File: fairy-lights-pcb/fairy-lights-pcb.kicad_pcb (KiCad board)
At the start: 2 copper layers, 60 x 60 mm, 19 parts, among them J1 Power_Jack, J2 Conn_LED_Strand_SPI, J3 Conn_LED_Strand_WS2812, J4 Conn_I2C, J5 Conn_02x04_Top_Bottom, SW1 SW_PWR, SW2 USER_A, SW3 USER_B, U1 WeMos_D1_mini

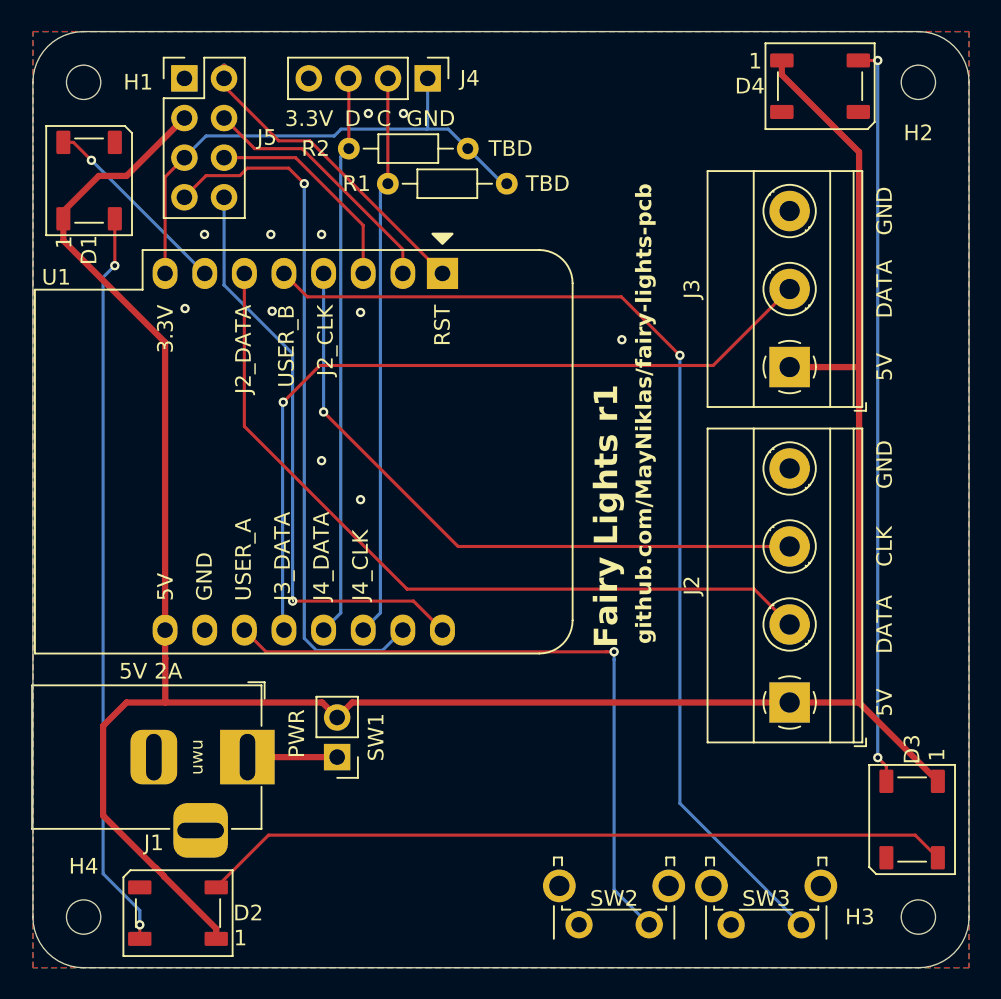
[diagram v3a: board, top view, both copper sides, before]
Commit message: Tweak MCU pin assignment
- Swaps the J3_DATA and USER_B pins.
- Now, all LED strand terminals and the I2C header are connected to GPIO
  pins with no strings (or, more accurately, random components on the
  MCU module) attached.
- Button USER_B puts the MCU flash mode if pressed at boot-up. The same
  can be achieved via USB, but, I guess, it's useful for flashing in the
  field with no USB but a UART?
- Button USER_A is tied to the same pin that drives the MCU module's
  on-board LED. When USER_A is pressed, the LED lights up. It might be
  worthwhile to re-wire USER_A to MCU pin D0 in order to free the LED
  and allow using USER_A as a soft power button (although that would
  require regularly polling the button in software while the MCU is
  running).
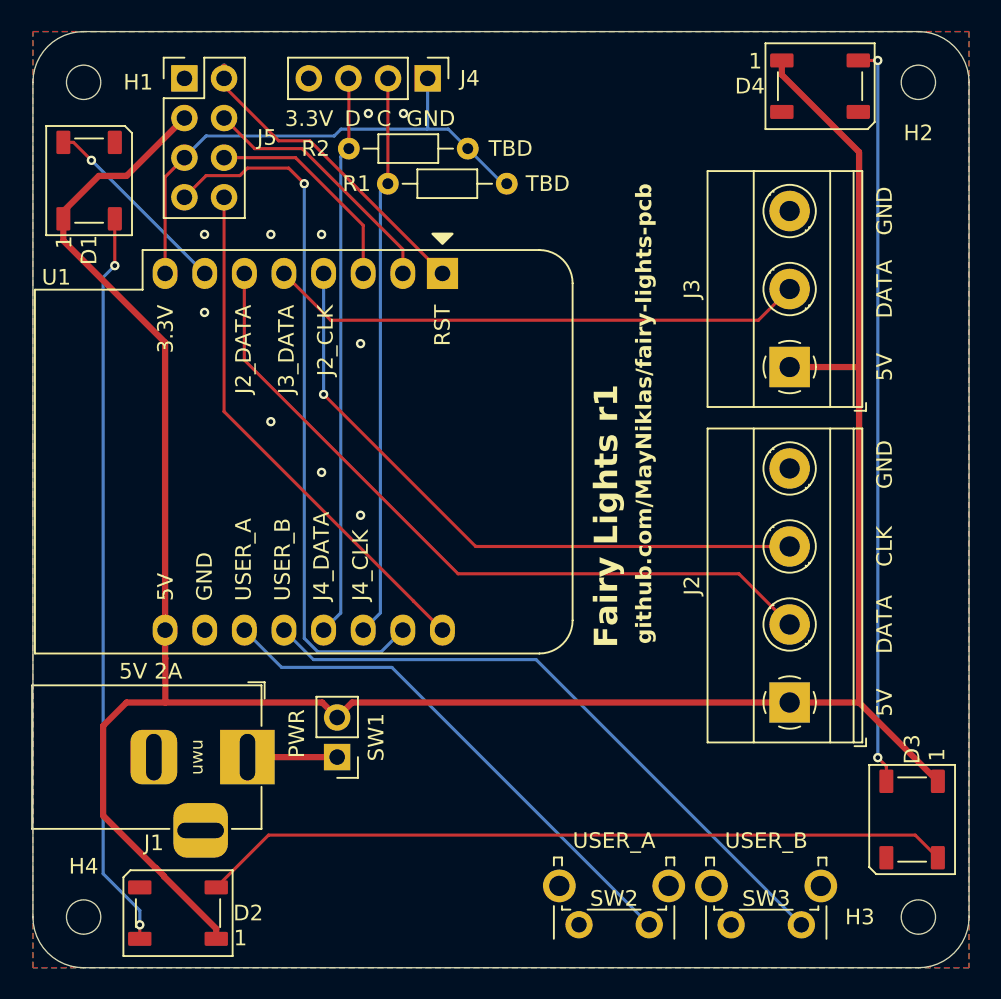
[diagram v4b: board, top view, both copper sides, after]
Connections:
- SW3 pad 1: Net-(U1-MISO/D6) -> Net-(U1-D3)
- U1 pad 12: Net-(J3-DATA) -> Net-(U1-D3)
- U1 pad 5: Net-(U1-MISO/D6) -> Net-(J3-DATA)
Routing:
- net Net-(U1-MISO/D6): track 67.3 -> 0.00 mm, vias 1 -> 0
- net Net-(U1-D3): track 0.00 -> 41.1 mm
- net Net-(J3-DATA): track 50.1 -> 34.5 mm, vias 1 -> 0
- net Net-(U1-D4): track 42.7 -> 33.8 mm, vias 1 -> 0
- net UC_TX: track 38.1 -> 33.5 mm, vias 1 -> 0
- net Net-(J2-DATA): track 50.0 -> 47.5 mm
- net Net-(J2-CLK): track 42.3 -> 41.7 mm
- net GND: vias 11 -> 10
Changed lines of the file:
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@@
 	(net 12 "UC_A0")
 	(net 13 "UC_D0")
-	(net 14 "Net-(U1-MISO{slash}D6)")
+	(net 14 "Net-(U1-D3)")
 	(net 15 "Net-(U1-D4)")
 	(net 16 "Net-(J4-CLK)")
@@
 		(property "Value" "USER_A"
 			(at 2.25 5.38988 180)
-			(layer "F.Fab")
+			(layer "F.SilkS")
 			(effects
 				(font
@@
 			(layers "*.Cu" "*.Mask")
 			(remove_unused_layers no)
-			(net 14 "Net-(U1-MISO{slash}D6)")
+			(net 6 "Net-(J3-DATA)")
 			(pinfunction "MISO/D6")
 			(pintype "bidirectional")
@@
 			(layers "*.Cu" "*.Mask")
 			(remove_unused_layers no)
-			(net 6 "Net-(J3-DATA)")
+			(net 14 "Net-(U1-D3)")
 			(pinfunction "D3")
 			(pintype "bidirectional")
@@
 		(property "Value" "USER_B"
 			(at 2.25 5.38988 180)
-			(layer "F.Fab")
+			(layer "F.SilkS")
 			(effects
 				(font
@@
 			(layers "*.Cu" "*.Mask")
 			(remove_unused_layers no)
-			(net 14 "Net-(U1-MISO{slash}D6)")
+			(net 14 "Net-(U1-D3)")
 			(pinfunction "1")
 			(pintype "passive")
@@
 		)
 	)
-	(gr_text "USER_B"
+	(gr_text "J3_DATA"
 		(at 76.25 77.5 90)
 		(layer "F.SilkS")
@@
 		)
 	)
-	(gr_text "J3_DATA"
+	(gr_text "USER_B"
 		(at 76 96.5 90)
 		(layer "F.SilkS")
@@
 	)
 	(via
-		(at 81 78)
+		(at 75.25 85)
 		(size 0.6)
 		(drill 0.3)
@@
 	)
 	(via
-		(at 75.332107 77.917893)
+		(at 78.5 73)
 		(size 0.6)
 		(drill 0.3)
@@
 	)
 	(via
-		(at 78.5 87.5)
+		(at 78.5 88.25)
 		(size 0.6)
 		(drill 0.3)
@@
 	)
 	(via
-		(at 78.5 73)
+		(at 81.5 65.25)
 		(size 0.6)
 		(drill 0.3)
@@
 	)
 	(via
-		(at 81.5 65.25)
+		(at 81 80)
 		(size 0.6)
 		(drill 0.3)
@@
 	)
 	(via
-		(at 71 73)
+		(at 81 91)
 		(size 0.6)
 		(drill 0.3)
@@
 	)
 	(via
-		(at 97.75 79.75)
+		(at 71 73)
 		(size 0.6)
 		(drill 0.3)
@@
 	)
 	(via
-		(at 69.75 77.75)
+		(at 71 78)
 		(size 0.6)
 		(drill 0.3)
@@
 		(net 2)
 	)
-	(via
-		(at 81 90)
-		(size 0.6)
-		(drill 0.3)
-		(layers "F.Cu" "B.Cu")
-		(free yes)
-		(net 2)
-	)
 	(segment
-		(start 83.983 95.733)
-		(end 73.55 85.3)
+		(start 108.5 98)
+		(end 105.25 94.75)
 		(width 0.2)
 		(layer "F.Cu")
@@
 	)
 	(segment
-		(start 108.5 98)
-		(end 106.233 95.733)
+		(start 73.55 81.05)
+		(end 73.55 75.5)
 		(width 0.2)
 		(layer "F.Cu")
@@
 	)
 	(segment
-		(start 73.55 85.3)
-		(end 73.55 75.5)
+		(start 87.25 94.75)
+		(end 73.55 81.05)
 		(width 0.2)
 		(layer "F.Cu")
@@
 	)
 	(segment
-		(start 106.233 95.733)
-		(end 83.983 95.733)
+		(start 105.25 94.75)
+		(end 87.25 94.75)
 		(width 0.2)
 		(layer "F.Cu")
@@
 	)
 	(segment
-		(start 87.25 93)
+		(start 88.38 93)
 		(end 108.5 93)
 		(width 0.2)
@@
 	)
 	(segment
-		(start 78.63 84.38)
-		(end 87.25 93)
+		(start 78.63 83.25)
+		(end 88.38 93)
 		(width 0.2)
 		(layer "F.Cu")
@@
 	)
 	(via
-		(at 78.63 84.38)
+		(at 78.63 83.25)
 		(size 0.6)
 		(drill 0.3)
@@
 	)
 	(segment
-		(start 78.63 84.38)
+		(start 78.63 83.25)
 		(end 78.63 75.5)
 		(width 0.2)
@@
 	)
 	(segment
-		(start 78.3956 81.3995)
-		(end 103.6005 81.3995)
+		(start 76.09 75.5)
+		(end 79.09 78.5)
 		(width 0.2)
 		(layer "F.Cu")
@@
 	)
 	(segment
-		(start 103.6005 81.3995)
+		(start 106.5 78.5)
 		(end 108.5 76.5)
 		(width 0.2)
@@
 	)
 	(segment
-		(start 76.0451 83.75)
-		(end 78.3956 81.3995)
+		(start 79.09 78.5)
+		(end 106.5 78.5)
 		(width 0.2)
 		(layer "F.Cu")
 		(net 6)
 	)
-	(via
-		(at 76.0451 83.75)
-		(size 0.6)
-		(drill 0.3)
-		(layers "F.Cu" "B.Cu")
-		(net 6)
-	)
-	(segment
-		(start 76 83.7951)
-		(end 76 98.27)
-		(width 0.2)
-		(layer "B.Cu")
-		(net 6)
-	)
-	(segment
-		(start 76 98.27)
-		(end 76.09 98.36)
-		(width 0.2)
-		(layer "B.Cu")
-		(net 6)
-	)
-	(segment
-		(start 76.0451 83.75)
-		(end 76 83.7951)
-		(width 0.2)
-		(layer "B.Cu")
-		(net 6)
-	)
 	(segment
 		(start 65.25 75)
@@
 	)
 	(segment
-		(start 76.6451 96.4997)
+		(start 84.3897 96.4946)
 		(end 84.3897 96.4997)
 		(width 0.2)
@@
 		(net 9)
 	)
-	(via
-		(at 76.6451 96.4997)
-		(size 0.6)
-		(drill 0.3)
-		(layers "F.Cu" "B.Cu")
-		(net 9)
-	)
-	(segment
-		(start 72.25 76.25)
-		(end 72.25 70.62)
-		(width 0.2)
-		(layer "B.Cu")
-		(net 9)
-	)
 	(segment
-		(start 76.6451 80.6451)
-		(end 72.25 76.25)
+		(start 72.25 84.3549)
+		(end 84.3897 96.4946)
 		(width 0.2)
-		(layer "B.Cu")
+		(layer "F.Cu")
 		(net 9)
 	)
 	(segment
-		(start 76.6451 96.4997)
-		(end 76.6451 80.6451)
+		(start 72.25 84.3549)
+		(end 72.25 70.62)
 		(width 0.2)
-		(layer "B.Cu")
+		(layer "F.Cu")
 		(net 9)
 	)
@@
 	)
 	(segment
-		(start 77.3925 69.75)
-		(end 77.3925 98.8897)
+		(start 82.32 99.75)
+		(end 83.71 98.36)
 		(width 0.2)
 		(layer "B.Cu")
@@
 	)
 	(segment
-		(start 77.3925 98.8897)
-		(end 78.1677 99.6649)
+		(start 78.2528 99.75)
+		(end 82.32 99.75)
 		(width 0.2)
 		(layer "B.Cu")
@@
 	)
 	(segment
-		(start 78.1677 99.6649)
-		(end 82.4051 99.6649)
+		(start 77.3925 98.8897)
+		(end 78.2528 99.75)
 		(width 0.2)
 		(layer "B.Cu")
@@
 	)
 	(segment
-		(start 82.4051 99.6649)
-		(end 83.71 98.36)
+		(start 77.3925 69.75)
+		(end 77.3925 98.8897)
 		(width 0.2)
 		(layer "B.Cu")
@@
 	)
 	(segment
-		(start 77.59 77)
-		(end 76.09 75.5)
-		(width 0.2)
-		(layer "F.Cu")
-		(net 14)
-	)
-	(segment
-		(start 101.4672 80.75)
-		(end 97.7172 77)
+		(start 76 98.27)
+		(end 76.09 98.36)
 		(width 0.2)
-		(layer "F.Cu")
+		(layer "B.Cu")
 		(net 14)
 	)
 	(segment
-		(start 97.7172 77)
-		(end 77.59 77)
+		(start 77.98 100.25)
+		(end 76.09 98.36)
 		(width 0.2)
-		(layer "F.Cu")
-		(net 14)
-	)
-	(via
-		(at 101.4672 80.75)
-		(size 0.6)
-		(drill 0.3)
-		(layers "F.Cu" "B.Cu")
+		(layer "B.Cu")
 		(net 14)
 	)
 	(segment
-		(start 101.4672 80.75)
-		(end 101.4672 109.4672)
+		(start 109.25 117.25)
+		(end 92.25 100.25)
 		(width 0.2)
 		(layer "B.Cu")
@@
 	)
 	(segment
-		(start 101.4672 109.4672)
-		(end 109.25 117.25)
+		(start 92.25 100.25)
+		(end 77.98 100.25)
 		(width 0.2)
 		(layer "B.Cu")
@@
 	)
 	(segment
-		(start 96.75 99.75)
-		(end 97.25 99.75)
-		(width 0.2)
-		(layer "F.Cu")
-		(net 15)
-	)
-	(segment
-		(start 96.75 99.75)
-		(end 74.94 99.75)
-		(width 0.2)
-		(layer "F.Cu")
-		(net 15)
-	)
-	(segment
-		(start 74.94 99.75)
-		(end 73.55 98.36)
-		(width 0.2)
-		(layer "F.Cu")
-		(net 15)
-	)
-	(via
-		(at 97.25 99.75)
-		(size 0.6)
-		(drill 0.3)
-		(layers "F.Cu" "B.Cu")
-		(net 15)
-	)
-	(segment
-		(start 97.25 100.25)
-		(end 97.25 114.9941)
+		(start 83.0059 100.75)
+		(end 99.5 117.2441)
 		(width 0.2)
 		(layer "B.Cu")
@@
 	)
 	(segment
-		(start 97.25 114.9941)
-		(end 99.5 117.2441)
+		(start 75.94 100.75)
+		(end 83.0059 100.75)
 		(width 0.2)
 		(layer "B.Cu")
@@
 	)
 	(segment
-		(start 97.25 100.25)
-		(end 97.25 99.75)
+		(start 73.55 98.36)
+		(end 75.94 100.75)
 		(width 0.2)
 		(layer "B.Cu")

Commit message: Fix component labels and positions
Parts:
- R1, R2: value TBD -> 10k
- moved J1 0.25 mm to (74.0, 106.5)
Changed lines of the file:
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@@
 			)
 		)
-		(property "Value" "TBD"
+		(property "Value" "10k"
 			(at -2.75 0 0)
 			(layer "F.SilkS")
@@
 			)
 		)
-		(property "Value" "TBD"
+		(property "Value" "10k"
 			(at 10.25 0 0)
 			(layer "F.SilkS")
@@
 	(footprint "Connector_BarrelJack:BarrelJack_Horizontal"
 		(layer "F.Cu")
-		(at 73.75 106.5)
+		(at 74 106.5)
 		(descr "DC Barrel Jack")
 		(tags "Power Jack")
@@
 		)
 		(property "Value" "USER_A"
-			(at 2.25 5.38988 180)
+			(at 2.25 4.9941 180)
 			(layer "F.SilkS")
 			(effects
@@
 		)
 		(property "Value" "USER_B"
-			(at 2.25 5.38988 180)
+			(at 2.25 5 180)
 			(layer "F.SilkS")
 			(effects
@@
 		(layer "Edge.Cuts")
 	)
-	(gr_text "GND"
+	(gr_text "3.3V"
 		(at 85.5 65 0)
 		(layer "F.SilkS")
@@
 		)
 	)
-	(gr_text "3.3V"
+	(gr_text "GND"
 		(at 77.7 65 0)
 		(layer "F.SilkS")
@@
 	)
 	(gr_text "5V 2A"
-		(at 67.55 101 0)
+		(at 67.75 101 0)
 		(layer "F.SilkS")
 		(effects
@@
 	)
 	(gr_text "PWR"
-		(at 77.5 105 90)
+		(at 77.75 105.25 90)
 		(layer "F.SilkS")
 		(effects
@@
 	)
 	(gr_text "uwu"
-		(at 70.5 106.5 90)
+		(at 70.75 106.5 90)
 		(layer "F.SilkS")
 		(effects
@@
 	)
 	(segment
-		(start 73.75 106.5)
+		(start 74 106.5)
 		(end 79.5 106.5)
 		(width 0.4)

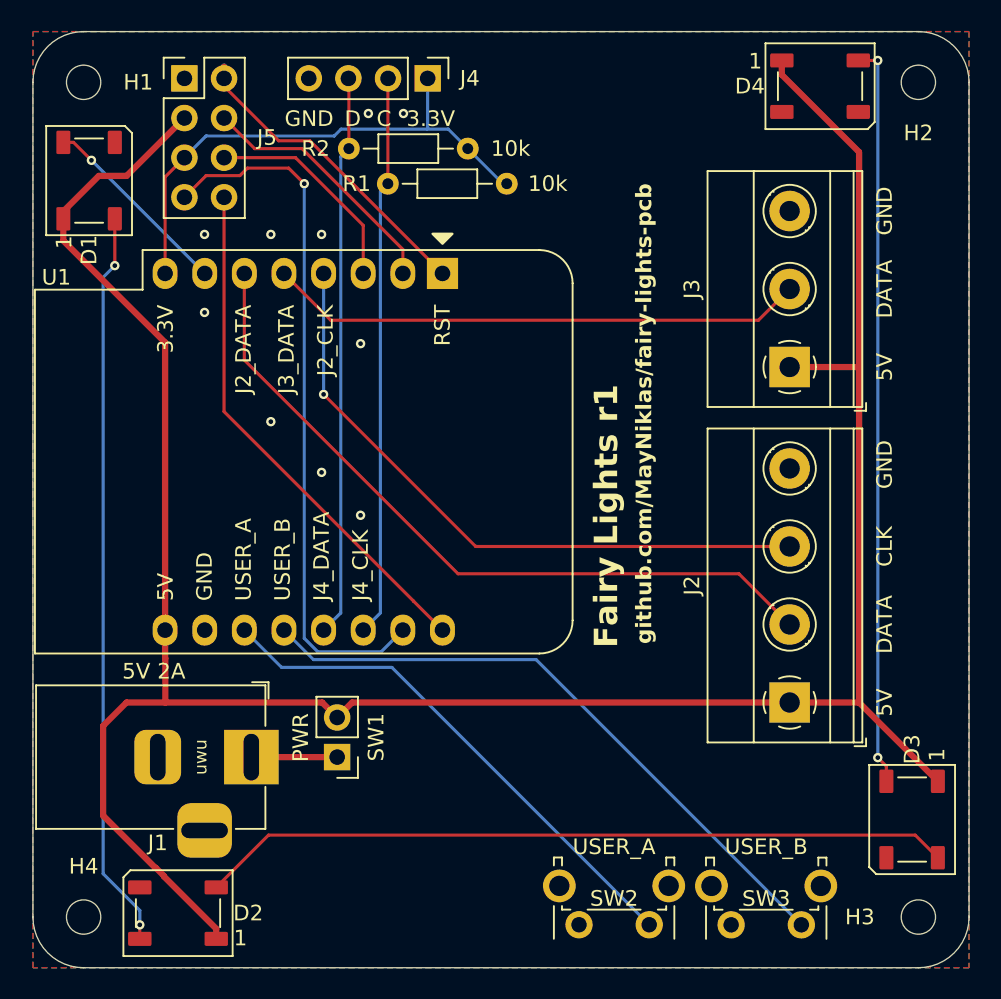
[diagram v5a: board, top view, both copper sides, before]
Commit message: Move USER_A button to pin D0
This allows using it to wake out of deep sleep, and avoids interactions
with the MCU module's built-in LED. The downside is that the pin has to
be polled in software while the MCU is running.
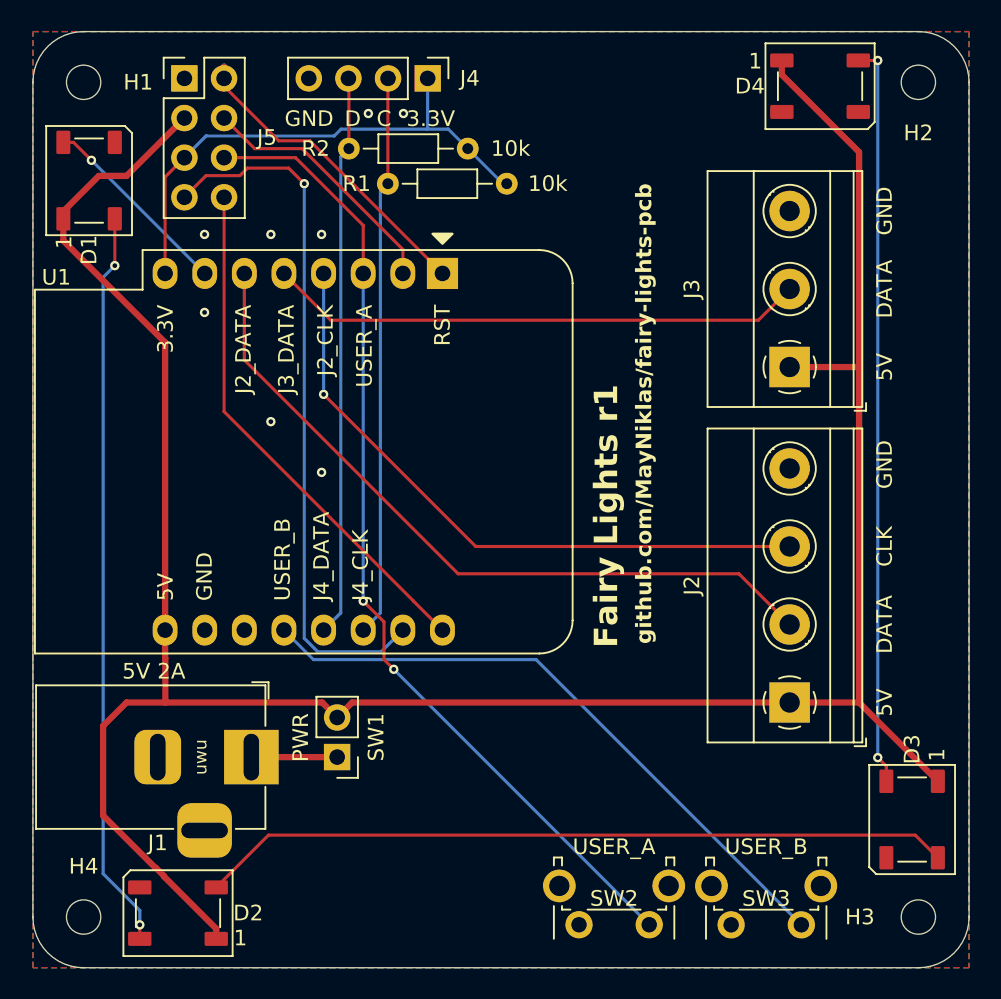
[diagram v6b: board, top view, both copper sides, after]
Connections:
- SW2 pad 1: Net-(U1-D4) -> UC_D0
- U1 pad 11: Net-(U1-D4) -> unconnected-(U1-D4-Pad11)
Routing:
- net UC_D0: track 13.8 -> 63.1 mm, vias 0 -> 2
- net Net-(U1-D4): track 33.8 -> 0.00 mm
- net GND: vias 10 -> 8
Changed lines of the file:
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@@
 	(net 13 "UC_D0")
 	(net 14 "Net-(U1-D3)")
-	(net 15 "Net-(U1-D4)")
+	(net 15 "unconnected-(U1-D4-Pad11)")
 	(net 16 "Net-(J4-CLK)")
 	(net 17 "Net-(J4-DATA)")
@@
 			(layers "*.Cu" "*.Mask")
 			(remove_unused_layers no)
-			(net 15 "Net-(U1-D4)")
+			(net 13 "UC_D0")
 			(pinfunction "1")
 			(pintype "passive")
@@
 			(layers "*.Cu" "*.Mask")
 			(remove_unused_layers no)
-			(net 15 "Net-(U1-D4)")
+			(net 15 "unconnected-(U1-D4-Pad11)")
 			(pinfunction "D4")
-			(pintype "bidirectional")
+			(pintype "bidirectional+no_connect")
 		)
 		(pad "12" thru_hole oval
@@
 	)
 	(gr_text "USER_A"
-		(at 73.5 96.5 90)
+		(at 81.25 77.5 90)
 		(layer "F.SilkS")
 		(effects
@@
 				(thickness 0.1)
 			)
-			(justify left)
+			(justify right)
 		)
 	)
@@
 	)
 	(via
-		(at 81 80)
-		(size 0.6)
-		(drill 0.3)
-		(layers "F.Cu" "B.Cu")
-		(free yes)
-		(net 2)
-	)
-	(via
-		(at 81 91)
-		(size 0.6)
-		(drill 0.3)
-		(layers "F.Cu" "B.Cu")
-		(free yes)
-		(net 2)
-	)
-	(via
 		(at 71 73)
 		(size 0.6)
@@
 	)
 	(segment
+		(start 82.5 100.2441)
+		(end 82.5 97.83)
+		(width 0.2)
+		(layer "F.Cu")
+		(net 13)
+	)
+	(segment
 		(start 81.17 75.5)
 		(end 81.17 72.42)
@@
 	)
 	(segment
+		(start 82.5 97.83)
+		(end 81.17 96.5)
+		(width 0.2)
+		(layer "F.Cu")
+		(net 13)
+	)
+	(segment
+		(start 83.12795 100.87205)
+		(end 82.5 100.2441)
+		(width 0.2)
+		(layer "F.Cu")
+		(net 13)
+	)
+	(segment
 		(start 76.83 68.08)
 		(end 72.25 68.08)
@@
 		(net 13)
 	)
+	(via
+		(at 83.12795 100.87205)
+		(size 0.6)
+		(drill 0.3)
+		(layers "F.Cu" "B.Cu")
+		(net 13)
+	)
+	(via
+		(at 81.17 96.5)
+		(size 0.6)
+		(drill 0.3)
+		(layers "F.Cu" "B.Cu")
+		(net 13)
+	)
+	(segment
+		(start 83.12795 100.87205)
+		(end 99.5 117.2441)
+		(width 0.2)
+		(layer "B.Cu")
+		(net 13)
+	)
+	(segment
+		(start 81.17 96.5)
+		(end 81.17 75.5)
+		(width 0.2)
+		(layer "B.Cu")
+		(net 13)
+	)
 	(segment
 		(start 76 98.27)
@@
 	)
 	(segment
-		(start 83.0059 100.75)
-		(end 99.5 117.2441)
-		(width 0.2)
-		(layer "B.Cu")
-		(net 15)
-	)
-	(segment
-		(start 75.94 100.75)
-		(end 83.0059 100.75)
-		(width 0.2)
-		(layer "B.Cu")
-		(net 15)
-	)
-	(segment
-		(start 73.55 98.36)
-		(end 75.94 100.75)
-		(width 0.2)
-		(layer "B.Cu")
-		(net 15)
-	)
-	(segment
